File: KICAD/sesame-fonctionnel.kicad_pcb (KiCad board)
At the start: 2 copper layers, 160 x 100 mm, 276 parts, among them J1 CXS70-14-C, J2 CXS70-14-C, J7 CXS70-14-C, J8 CXS70-14-C, J9 Conn_02x16_Odd_Even, Q1 BC847, Q10 BC857, Q11 SQM120, Q12 BC847, Q13 BC847, Q2 BC847, Q3 BC847, Q4 BC847, Q5 BC847, Q6 SQM120, Q7 BC857, Q8 SQM120, Q9 SQM120, U1 AD8030, U10 LT6016, U11 AD8030, U12 UCC27284-Q1, U13 AD8030, U14 AD8030, U15 LT8365, U16 LM4040DBZ-2.5, U17 UCC27284-Q1, U2 LM2903, U3 CD4053BM96, U4 4011, U5 CD4053BM96, U6 CD4053BM96, U7 AD8030, U8 LT6016, U9 AD8030

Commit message: end of placement 7 beginning of routing
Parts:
- added C50: 1uF, Sesame_footprint:C_0805_2012Metric_Pad1.18x1.45mm_HandSolder, F.Cu at (110.5, 52.9)
- added C51: 1uF, Sesame_footprint:C_0805_2012Metric_Pad1.18x1.45mm_HandSolder, F.Cu at (121.0, 184.0)
- moved D13 298.8 mm to (168.2, 56.7), turned to 0 degrees
- moved TP39 224.3 mm to (85.1, 90.3), turned to 90 degrees
- moved TP41 222.4 mm to (95.2, 71.3), turned to 90 degrees
- moved TP42 220.3 mm to (101.6, 65.5), turned to 90 degrees
- moved R82 219.1 mm to (106.0, 82.1), turned to 270 degrees
- moved R81 217.5 mm to (106.0, 76.3), turned to 270 degrees
- moved R12 215.6 mm to (127.0, 122.7), turned to 90 degrees
- moved R13 212.0 mm to (123.2, 122.7), turned to 270 degrees
- moved C31 211.5 mm to (98.4, 89.0), turned to 270 degrees
- moved TP40 209.5 mm to (85.1, 71.3), turned to 90 degrees
- moved R19 209.2 mm to (127.0, 117.6), turned to 270 degrees
- moved RV3 207.8 mm to (119.3, 122.7), turned to 90 degrees
- moved U15 206.1 mm to (100.8, 82.6), turned to 90 degrees
- moved R18 205.2 mm to (123.2, 117.6), turned to 270 degrees
- moved C32 204.9 mm to (101.6, 71.3), turned to 180 degrees
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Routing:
- net /PID/PID_Setpoint: track 0.00 -> 36.2 mm
- net Net-(R40-Pad1): track 0.00 -> 18.8 mm
- net Net-(C18-Pad2): track 0.00 -> 13.6 mm
- net /PWM GEN/VDeadTime: track 0.00 -> 12.8 mm
- net /PWM GEN/Ramp: track 7.40 -> 18.9 mm
- net /RAMP GENERATOR/Triangle_offset: track 0.00 -> 10.0 mm
- net /PID/Feedback_raw: track 3.03 -> 11.6 mm
- net Net-(R39-Pad1): track 0.00 -> 7.96 mm
- net GND: track 0.00 -> 7.78 mm, vias 0 -> 4
- net /RAMP GENERATOR/Schmitt_offset: track 0.00 -> 6.80 mm
- net Net-(C28-Pad1): track 0.00 -> 6.60 mm
- net Net-(C31-Pad1): track 0.00 -> 5.51 mm
- net /MOS DRIVER L/VS: track 0.00 -> 5.07 mm
- net Net-(JP9-Pad1): track 0.00 -> 4.08 mm
- net Net-(JP8-Pad1): track 0.00 -> 4.08 mm
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- added copper zone on F.Cu, net /INTERNAL SUPPLIES/VIN
- added copper zone on B.Cu, net GND
- added copper zone on F.Cu, net GND
- added copper zone on F.Cu, net Net-(C30-Pad2)
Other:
- net class Big_Pwr added: clearance 1, trace_width 3, via_dia 1.6, via_drill 1
- net class Default: via_dia 0.8 -> 0.82
- net class VCC added: clearance 0.2, trace_width 1, via_dia 0.82, via_drill 0.4
- rule trace_min: 0.2 -> 0.21
- rule via_min_drill: 0.3 -> 0.4
- rule via_min_size: 0.4 -> 0.82
- board text added: "VREF"
- board text added: "driver"
- board text removed: "Driver L"
- board text removed: "Driver R"
- board text removed: "Prog. breaker"

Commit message: changed monting holes + tweaks & still routing
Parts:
- H1, H2, H3, H4: footprint MountingHole:MountingHole_3.2mm_M3 -> Sesame_footprint:MountingHole_3.2mm_M3
- U3, U5, U6: footprint Package_SO:SOIC-16_4.55x10.3mm_P1.27mm -> Package_SO:SOIC-16_3.9x9.9mm_P1.27mm
- moved JP10 95.8 mm to (139.0, 82.1), turned to 270 degrees
- moved JP11 91.2 mm to (139.0, 85.9), turned to 270 degrees
- moved C42 68.3 mm to (202.5, 125.9)
- moved R92 56.1 mm to (208.2, 125.9)
- moved R91 54.4 mm to (175.2, 125.9)
- moved C41 47.0 mm to (170.2, 125.9)
- moved TP2 30.5 mm to (139.0, 104.9)
- moved TP4 19.3 mm to (135.2, 104.9)
- moved JP12 16.8 mm to (71.7, 117.6)
- moved TP7 16.5 mm to (97.3, 134.1)
- moved Q4 12.7 mm to (163.8, 153.2), turned to 180 degrees
- moved Q5 12.7 mm to (151.1, 153.2), turned to 0 degrees
- moved JP16 10.6 mm to (71.7, 78.9), turned to 90 degrees
- moved R73 10.0 mm to (122.5, 104.9), turned to 270 degrees
- moved R71 9.74 mm to (126.3, 95.4), turned to 90 degrees
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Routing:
- net /INT EXT CONFIG/Ext_PWM: track 0.00 -> 81.7 mm
- net /INT EXT CONFIG/~Ext_PWM: track 0.00 -> 75.6 mm
- net /PID/Feedback: track 0.00 -> 44.0 mm
- net /PWM GEN/Ramp: track 18.9 -> 54.6 mm, vias 0 -> 1
- net Net-(C9-Pad2): track 7.62 -> 36.6 mm
- net Net-(C7-Pad2): track 7.62 -> 32.9 mm
- net /PWM GEN/Feedback_Deadtime: track 0.00 -> 20.5 mm
- net /INT_PWM_Power: track 0.00 -> 20.2 mm
- net Net-(Q5-Pad3): track 0.00 -> 19.1 mm, vias 0 -> 3
- net /~INT_PWM_Freewheel: track 0.00 -> 18.9 mm
- net /DC/DC CONVERTER/VD_LS: track 0.00 -> 12.9 mm
- net Net-(R39-Pad1): track 7.96 -> 20.8 mm
- net Net-(R72-Pad2): track 3.08 -> 14.2 mm
- net Net-(C8-Pad1): track 0.00 -> 10.1 mm
- net /DC/DC CONVERTER/VG_LS: track 0.00 -> 9.89 mm
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- added copper zone on F.Cu, net /U/I SENSOR RIGHT/VD_Mos
- added copper zone on F.Cu, net Net-(C30-Pad1)
- added copper zone on F.Cu, net VCC
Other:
- net class Big_Pwr: trace_width 3 -> 2.999999
- board text added: "ALEEA 2021 SESAME REV. A"
- board text added: "copie protect"
- board text added: "copie ui sens"
- board text removed: "ALEEA 2021"

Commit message: protect left finished
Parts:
- moved TP22 18.2 mm to (138.4, 146.8)
- moved TP21 15.3 mm to (132.7, 151.9)
- moved TP9 9.52 mm to (111.1, 153.8)
- moved C12 8.98 mm to (105.0, 139.2)
- moved R54 8.91 mm to (185.4, 156.4), turned to 180 degrees
- moved TP24 7.73 mm to (196.8, 155.7)
- moved TP20 5.75 mm to (167.0, 157.0)
- moved D4 3.24 mm to (191.1, 156.4), turned to 180 degrees
- moved Q7 2.57 mm to (174.9, 153.2)
- moved C13 1.91 mm to (94.0, 146.2)
- moved D3 1.47 mm to (179.7, 156.4)
- moved C11 1.27 mm to (104.7, 131.6)
- moved Q3 1.27 mm to (108.6, 131.6)
- moved TP25 0.90 mm to (173.3, 144.9)
- moved D2 0.90 mm to (202.5, 156.4)
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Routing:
- net Net-(D2-Pad1): track 0.00 -> 40.3 mm
- net Net-(D2-Pad2): track 0.00 -> 30.0 mm, vias 0 -> 2
- net Net-(D4-Pad2): track 0.00 -> 22.8 mm
- net Net-(D3-Pad1): track 0.00 -> 12.3 mm
- net Net-(Q7-Pad1): track 0.00 -> 4.36 mm
- net /VProt_Left: track 7.62 -> 3.81 mm
- net VCC: track 0.00 -> 3.32 mm
- net Net-(R49-Pad2): track 3.08 -> 0.00 mm
- net GND: track 16.3 -> 19.3 mm, vias 9 -> 10
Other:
- board text added: "Protect"

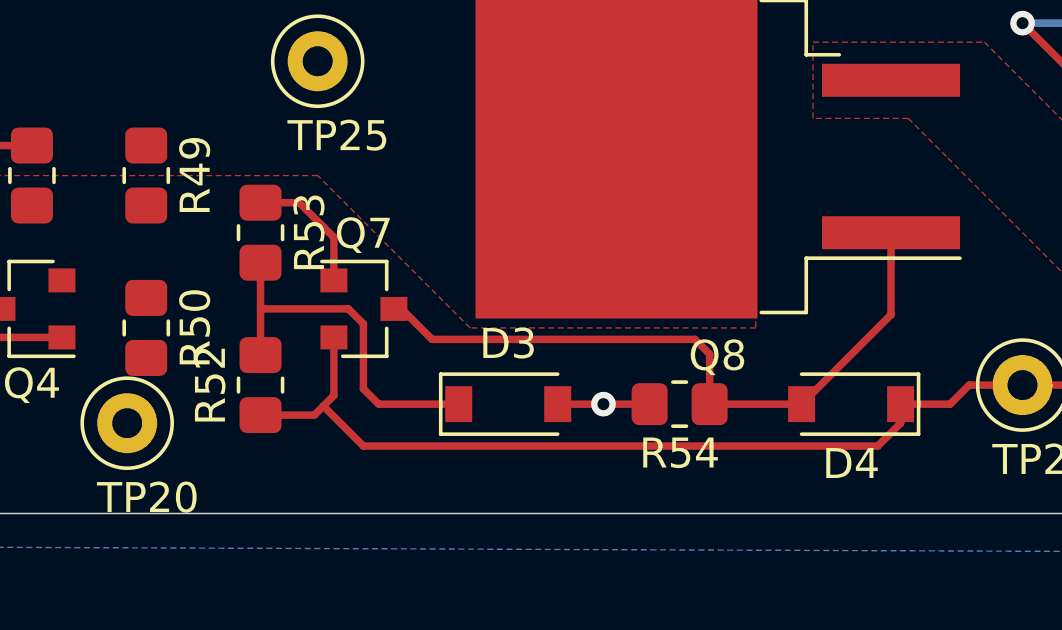
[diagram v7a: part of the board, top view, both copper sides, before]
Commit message: changed transistor placement in protect
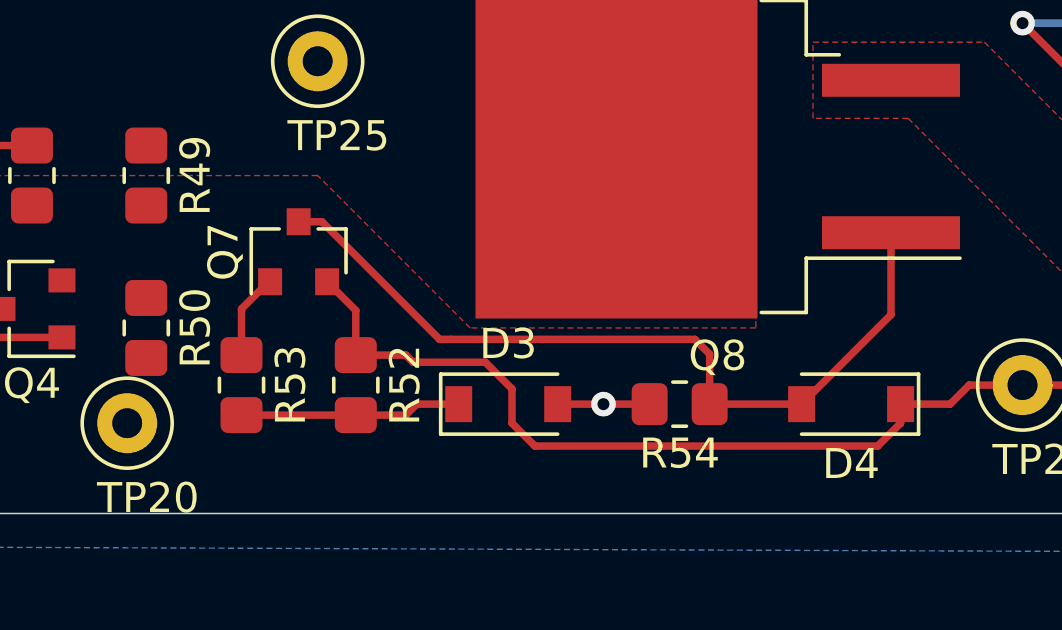
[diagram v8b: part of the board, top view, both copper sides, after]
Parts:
- moved R53 5.12 mm to (170.8, 155.7)
- moved R52 3.18 mm to (174.6, 155.7), turned to 270 degrees
- moved Q7 2.89 mm to (172.7, 151.3), turned to 90 degrees
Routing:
- net Net-(D3-Pad1): track 12.3 -> 7.39 mm
- net Net-(D4-Pad2): track 22.8 -> 27.2 mm
- net Net-(D2-Pad1): track 40.3 -> 38.8 mm
- net Net-(Q7-Pad1): track 4.36 -> 3.32 mm
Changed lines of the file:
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@@
     (thickness 1.6)
     (drawings 91)
-    (tracks 443)
+    (tracks 445)
     (zones 0)
     (modules 278)
@@
   )
   (module Sesame_footprint:R_0805_2012Metric_Pad1.20x1.40mm_HandSolder (layer F.Cu)
-    (at 171.42 155.72 90)
+    (at 174.595 155.72 270)
     (descr "Resistor SMD 0805 (2012 Metric), square (rectangular) end terminal, IPC_7351 nominal with elongated pad for handsoldering. (Body size source: IPC-SM-782 page 72, https://www.pcb-3d.com/wordpress/wp-content/uploads/ipc-sm-782a_amendment_1_and_2.pdf), generated with kicad-footprint-generator")
     (tags "resistor handsolder")
@@
       (effects (font (size 0.5 0.5) (thickness 0.08)))
     )
-    (pad 1 smd roundrect (at -1 0 90) (size 1.2 1.4) (layers F.Cu F.Paste F.Mask) (roundrect_rratio 0.208333)
+    (pad 1 smd roundrect (at -1 0 270) (size 1.2 1.4) (layers F.Cu F.Paste F.Mask) (roundrect_rratio 0.208333)
       (net 34 "Net-(D2-Pad1)"))
-    (pad 2 smd roundrect (at 1 0 90) (size 1.2 1.4) (layers F.Cu F.Paste F.Mask) (roundrect_rratio 0.208333)
+    (pad 2 smd roundrect (at 1 0 270) (size 1.2 1.4) (layers F.Cu F.Paste F.Mask) (roundrect_rratio 0.208333)
       (net 35 "Net-(D3-Pad1)"))
     (model ${KISYS3DMOD}/Resistor_SMD.3dshapes/R_0805_2012Metric.wrl
@@
   )
   (module Sesame_footprint:R_0805_2012Metric_Pad1.20x1.40mm_HandSolder (layer F.Cu)
-    (at 171.42 150.64 270)
+    (at 170.785 155.72 270)
     (descr "Resistor SMD 0805 (2012 Metric), square (rectangular) end terminal, IPC_7351 nominal with elongated pad for handsoldering. (Body size source: IPC-SM-782 page 72, https://www.pcb-3d.com/wordpress/wp-content/uploads/ipc-sm-782a_amendment_1_and_2.pdf), generated with kicad-footprint-generator")
     (tags "resistor handsolder")
@@
   )
   (module Package_TO_SOT_SMD:SOT-23 (layer F.Cu)
-    (at 174.865 153.18)
+    (at 172.69 151.275 90)
     (descr "SOT-23, Standard")
     (tags SOT-23)
     (attr smd)
-    (fp_text reference Q7 (at 0 -2.5) (layer F.SilkS)
+    (fp_text reference Q7 (at 0 -2.5 90) (layer F.SilkS)
       (effects (font (size 1 1) (thickness 0.15)))
     )
-    (fp_text value BC857 (at 0 2.5) (layer F.Fab)
+    (fp_text value BC857 (at 0 2.5 90) (layer F.Fab)
       (effects (font (size 1 1) (thickness 0.15)))
     )
@@
     (fp_line (start -0.15 -1.52) (end 0.7 -1.52) (layer F.Fab) (width 0.1))
     (fp_line (start -0.7 -0.95) (end -0.7 1.5) (layer F.Fab) (width 0.1))
-    (fp_text user %R (at 0 0 -270) (layer F.Fab)
+    (fp_text user %R (at 0 0) (layer F.Fab)
       (effects (font (size 0.5 0.5) (thickness 0.075)))
     )
-    (pad 3 smd rect (at 1 0) (size 0.9 0.8) (layers F.Cu F.Paste F.Mask)
+    (pad 3 smd rect (at 1 0 90) (size 0.9 0.8) (layers F.Cu F.Paste F.Mask)
       (net 36 "Net-(D4-Pad2)"))
-    (pad 2 smd rect (at -1 0.95) (size 0.9 0.8) (layers F.Cu F.Paste F.Mask)
+    (pad 2 smd rect (at -1 0.95 90) (size 0.9 0.8) (layers F.Cu F.Paste F.Mask)
       (net 34 "Net-(D2-Pad1)"))
-    (pad 1 smd rect (at -1 -0.95) (size 0.9 0.8) (layers F.Cu F.Paste F.Mask)
+    (pad 1 smd rect (at -1 -0.95 90) (size 0.9 0.8) (layers F.Cu F.Paste F.Mask)
       (net 90 "Net-(Q7-Pad1)"))
     (model ${KISYS3DMOD}/Package_TO_SOT_SMD.3dshapes/SOT-23.wrl
@@
   (segment (start 195.042 155.72) (end 194.407 156.355) (width 0.25) (layer F.Cu) (net 34))
   (segment (start 192.755 156.355) (end 194.407 156.355) (width 0.25) (layer F.Cu) (net 34))
-  (segment (start 173.865 154.13) (end 173.865 156.069) (width 0.25) (layer F.Cu) (net 34))
-  (segment (start 173.214 156.72) (end 171.42 156.72) (width 0.25) (layer F.Cu) (net 34))
-  (segment (start 174.849 157.752) (end 173.5155 156.4185) (width 0.25) (layer F.Cu) (net 34))
-  (segment (start 192.755 156.355) (end 192.755 156.991) (width 0.25) (layer F.Cu) (net 34))
-  (segment (start 173.5155 156.4185) (end 173.214 156.72) (width 0.25) (layer F.Cu) (net 34))
-  (segment (start 191.994 157.752) (end 174.849 157.752) (width 0.25) (layer F.Cu) (net 34))
-  (segment (start 192.755 156.991) (end 191.994 157.752) (width 0.25) (layer F.Cu) (net 34))
-  (segment (start 173.865 156.069) (end 173.5155 156.4185) (width 0.25) (layer F.Cu) (net 34))
   (segment (start 200.885 156.355) (end 199.233 156.355) (width 0.25) (layer F.Cu) (net 34))
   (segment (start 200.885 150.96) (end 201.205 150.64) (width 0.25) (layer F.Cu) (net 34))
   (segment (start 200.885 156.355) (end 200.885 150.96) (width 0.25) (layer F.Cu) (net 34))
-  (segment (start 174.350002 153.18) (end 174.849 153.678998) (width 0.25) (layer F.Cu) (net 35))
-  (segment (start 171.42 153.18) (end 174.350002 153.18) (width 0.25) (layer F.Cu) (net 35))
-  (segment (start 171.42 151.64) (end 171.42 153.18) (width 0.25) (layer F.Cu) (net 35))
-  (segment (start 171.42 153.18) (end 171.42 154.72) (width 0.25) (layer F.Cu) (net 35))
-  (segment (start 174.849 153.678998) (end 174.849 155.847) (width 0.25) (layer F.Cu) (net 35))
-  (segment (start 175.357 156.355) (end 178.025 156.355) (width 0.25) (layer F.Cu) (net 35))
-  (segment (start 174.849 155.847) (end 175.357 156.355) (width 0.25) (layer F.Cu) (net 35))
+  (segment (start 174.595 153.23) (end 173.64 152.275) (width 0.25) (layer F.Cu) (net 34))
+  (segment (start 174.595 154.72) (end 174.595 153.23) (width 0.25) (layer F.Cu) (net 34))
+  (segment (start 191.994 157.752) (end 180.564 157.752) (width 0.25) (layer F.Cu) (net 34))
+  (segment (start 178.913 154.958) (end 179.802 155.847) (width 0.25) (layer F.Cu) (net 34))
+  (segment (start 179.802 156.99) (end 180.564 157.752) (width 0.25) (layer F.Cu) (net 34))
+  (segment (start 179.802 155.847) (end 179.802 156.99) (width 0.25) (layer F.Cu) (net 34))
+  (segment (start 176.5 154.958) (end 178.913 154.958) (width 0.25) (layer F.Cu) (net 34))
+  (segment (start 192.755 156.355) (end 192.755 156.991) (width 0.25) (layer F.Cu) (net 34))
+  (segment (start 176.262 154.72) (end 176.5 154.958) (width 0.25) (layer F.Cu) (net 34))
+  (segment (start 192.755 156.991) (end 191.994 157.752) (width 0.25) (layer F.Cu) (net 34))
+  (segment (start 174.595 154.72) (end 176.262 154.72) (width 0.25) (layer F.Cu) (net 34))
+  (segment (start 174.595 156.72) (end 176.262 156.72) (width 0.25) (layer F.Cu) (net 35))
+  (segment (start 176.627 156.355) (end 178.025 156.355) (width 0.25) (layer F.Cu) (net 35))
+  (segment (start 176.262 156.72) (end 176.627 156.355) (width 0.25) (layer F.Cu) (net 35))
+  (segment (start 174.595 156.72) (end 170.785 156.72) (width 0.25) (layer F.Cu) (net 35))
   (segment (start 192.435 153.375) (end 189.455 156.355) (width 0.25) (layer F.Cu) (net 36))
   (segment (start 192.435 150.64) (end 192.435 153.375) (width 0.25) (layer F.Cu) (net 36))
   (segment (start 186.39 156.355) (end 189.455 156.355) (width 0.25) (layer F.Cu) (net 36))
-  (segment (start 175.865 153.18) (end 176.119 153.18) (width 0.25) (layer F.Cu) (net 36))
-  (segment (start 176.119 153.18) (end 177.135 154.196) (width 0.25) (layer F.Cu) (net 36))
-  (segment (start 177.135 154.196) (end 185.898 154.196) (width 0.25) (layer F.Cu) (net 36))
   (segment (start 186.39 154.688) (end 186.39 156.355) (width 0.25) (layer F.Cu) (net 36))
   (segment (start 185.898 154.196) (end 186.39 154.688) (width 0.25) (layer F.Cu) (net 36))
+  (segment (start 172.69 150.275) (end 173.468 150.275) (width 0.25) (layer F.Cu) (net 36))
+  (segment (start 173.468 150.275) (end 177.389 154.196) (width 0.25) (layer F.Cu) (net 36))
+  (segment (start 177.77 154.196) (end 185.898 154.196) (width 0.25) (layer F.Cu) (net 36))
+  (segment (start 177.389 154.196) (end 177.77 154.196) (width 0.25) (layer F.Cu) (net 36))
   (segment (start 172.115 136.67) (end 174.595 136.67) (width 0.25) (layer F.Cu) (net 43))
   (segment (start 176.5 138.575) (end 177.77 138.575) (width 0.25) (layer F.Cu) (net 43))
@@
   (segment (start 152.952501 152.597499) (end 152.952501 152.605911) (width 0.25) (layer F.Cu) (net 89))
   (segment (start 155.25 153.505) (end 153.823 153.505) (width 0.25) (layer F.Cu) (net 89))
-  (segment (start 171.42 149.64) (end 172.706 149.64) (width 0.25) (layer F.Cu) (net 90))
-  (segment (start 173.865 150.799) (end 173.865 152.23) (width 0.25) (layer F.Cu) (net 90))
-  (segment (start 172.706 149.64) (end 173.865 150.799) (width 0.25) (layer F.Cu) (net 90))
+  (segment (start 171.42 152.595) (end 171.74 152.275) (width 0.25) (layer F.Cu) (net 90))
+  (segment (start 171.74 152.275) (end 171.69 152.275) (width 0.25) (layer F.Cu) (net 90))
+  (segment (start 170.785 153.18) (end 170.785 154.72) (width 0.25) (layer F.Cu) (net 90))
+  (segment (start 171.69 152.275) (end 170.785 153.18) (width 0.25) (layer F.Cu) (net 90))
   (segment (start 135.86 118.62) (end 135.86 121.7) (width 0.25) (layer F.Cu) (net 97))
   (segment (start 139.67 121.7) (end 135.86 121.7) (width 0.25) (layer F.Cu) (net 97))
